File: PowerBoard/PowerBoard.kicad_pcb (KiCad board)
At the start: 2 copper layers, 95 x 72 mm, 24 parts, among them J1 AC_IN, J2 RelayCoil, J3 GATE_DRIVE, J4 LOGIC, J5 DC_LINK, K1 ALQ305

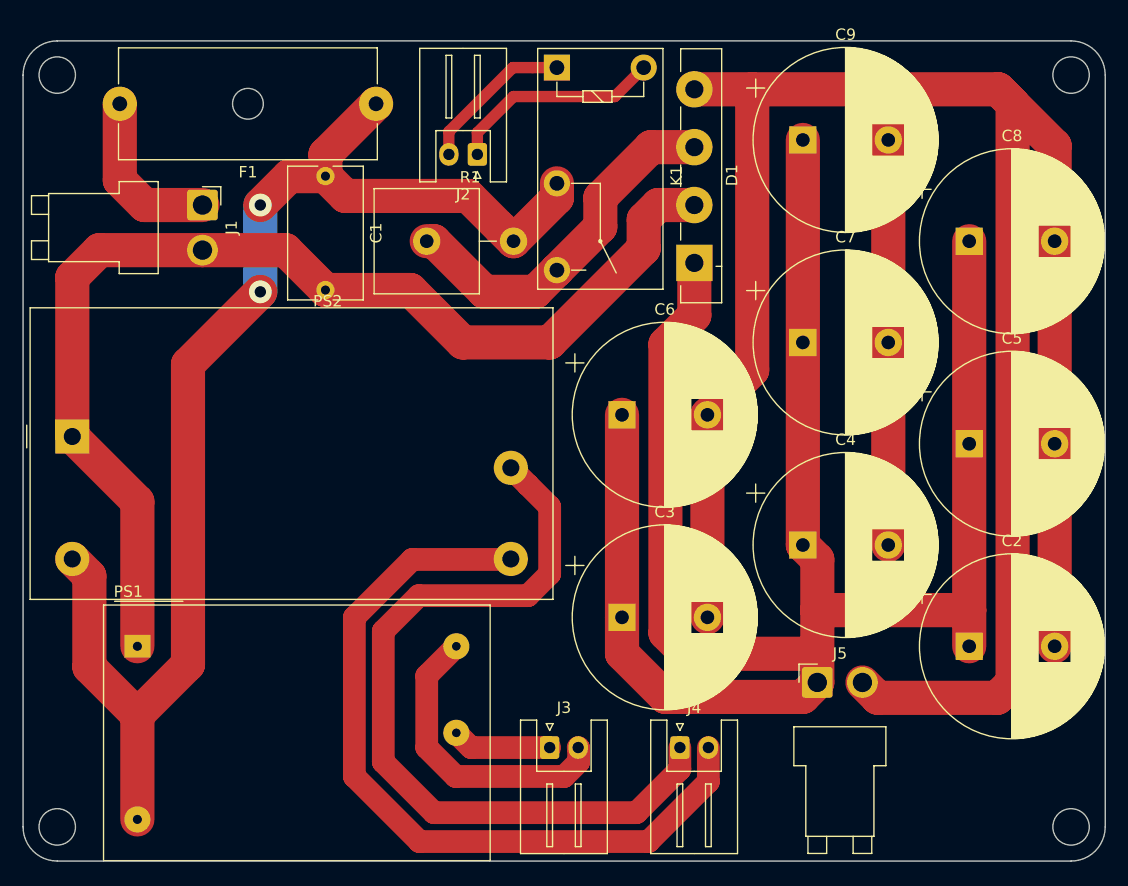
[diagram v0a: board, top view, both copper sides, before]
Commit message: コネクタ配置変更，シルク調整
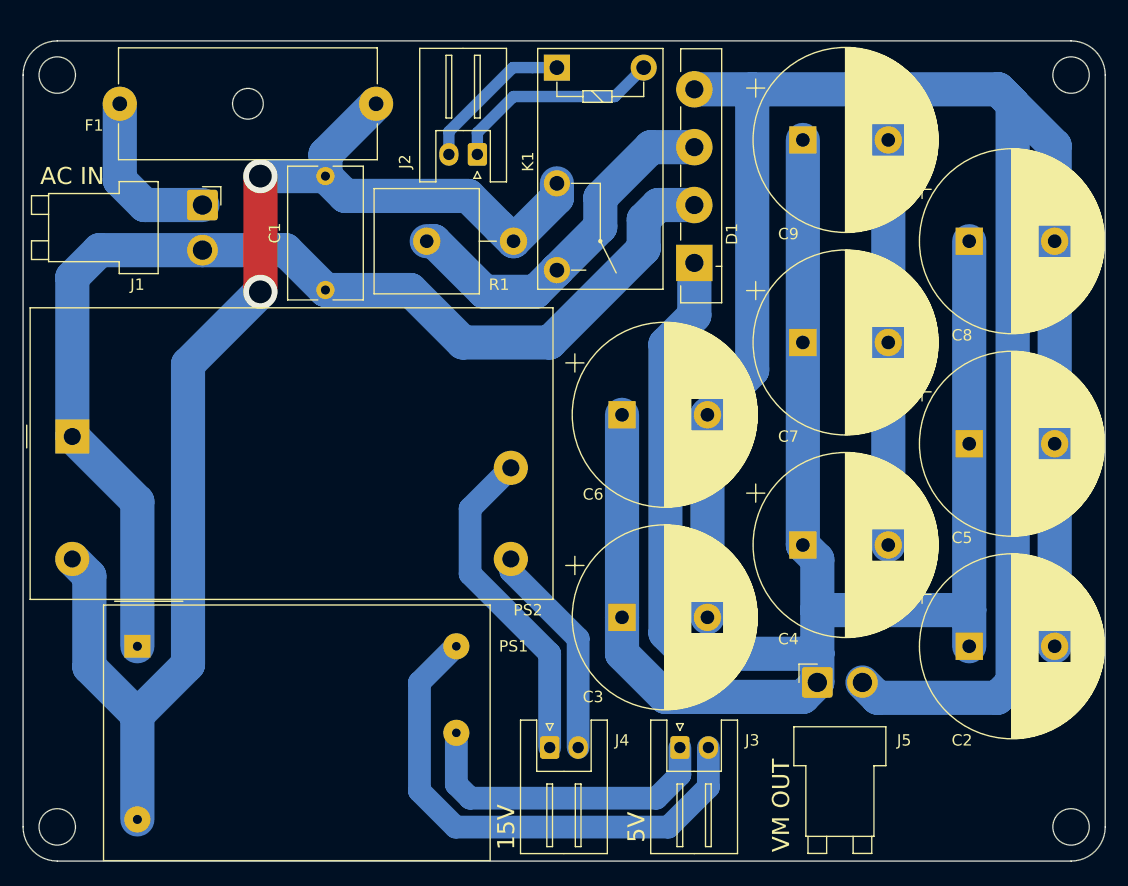
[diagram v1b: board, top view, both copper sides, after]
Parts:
- moved J3 11.4 mm to (10.2, 26.0)
- moved J4 11.4 mm to (-1.27, 26.0)
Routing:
- net Net-(J4-Pad2): track 68.4 -> 19.0 mm
- net Net-(J4-Pad1): track 70.3 -> 28.9 mm
- net Net-(J3-Pad2): track 26.2 -> 45.7 mm
- net Net-(J3-Pad1): track 8.73 -> 27.9 mm
- net Net-(C1-Pad1): track 115.0 -> 116.5 mm
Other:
- board text added: "15V"
- board text added: "5V"
- board text added: "AC IN"
- board text added: "VM OUT"

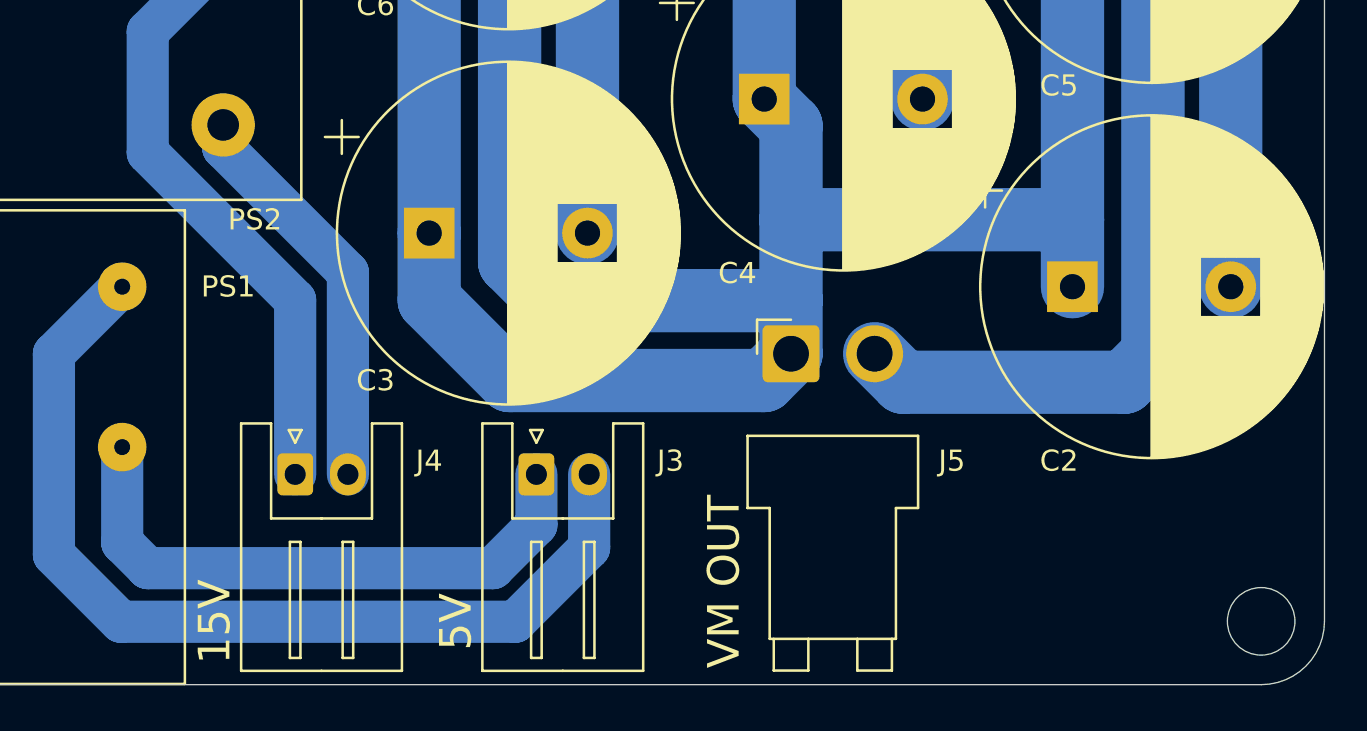
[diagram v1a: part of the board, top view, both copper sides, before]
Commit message: シルク調整
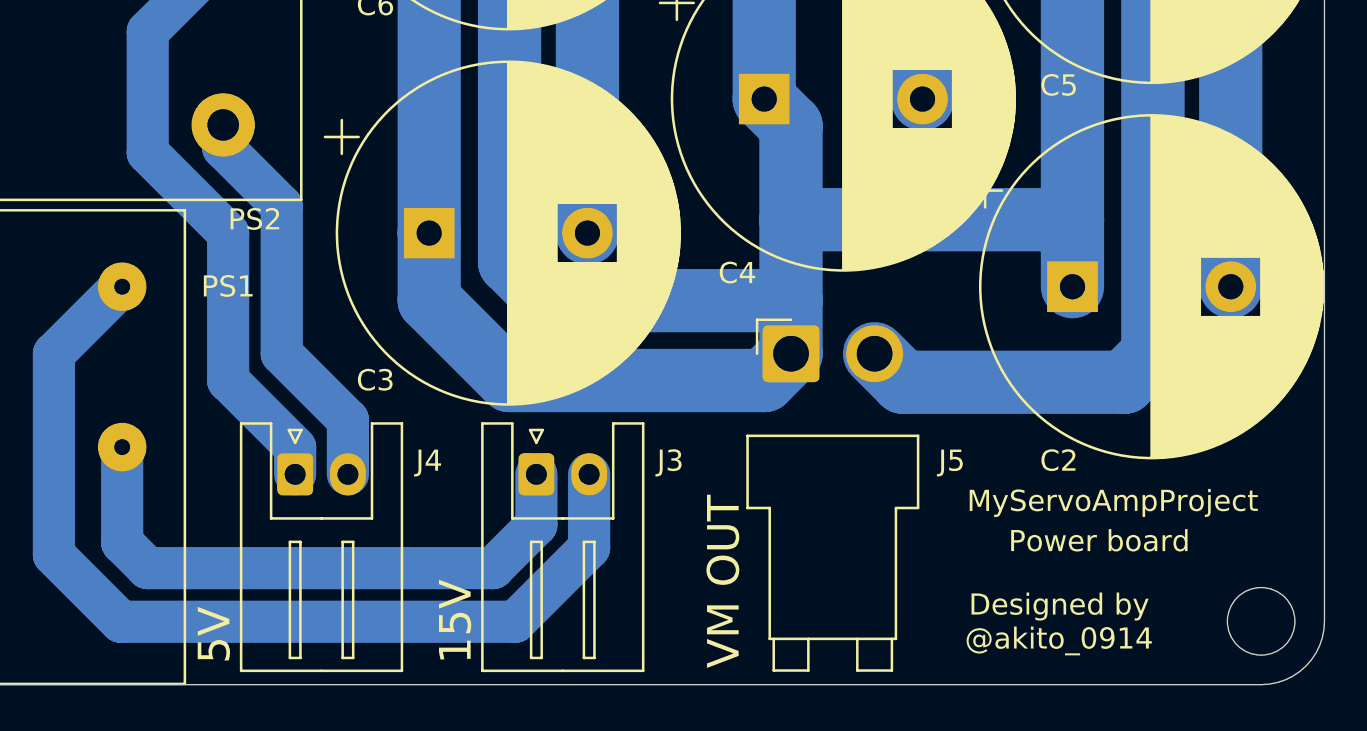
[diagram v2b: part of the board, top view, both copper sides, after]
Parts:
- added REF**: KiCad-Logo2_12mm_SilkScreen, Symbol:KiCad-Logo2_12mm_SilkScreen, B.Cu at (-24.1, 12.1)
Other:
- board text added: "Designed by @akito_0914"
- board text added: "MyServoAmpProject"
- board text added: "Power board"
